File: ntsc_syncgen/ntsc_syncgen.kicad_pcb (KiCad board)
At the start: 2 copper layers, 7 parts, among them U1 74HC4040D, U2 74HC4040D, U3 74HC7014, U4 74HC74D, Y1 Crystal

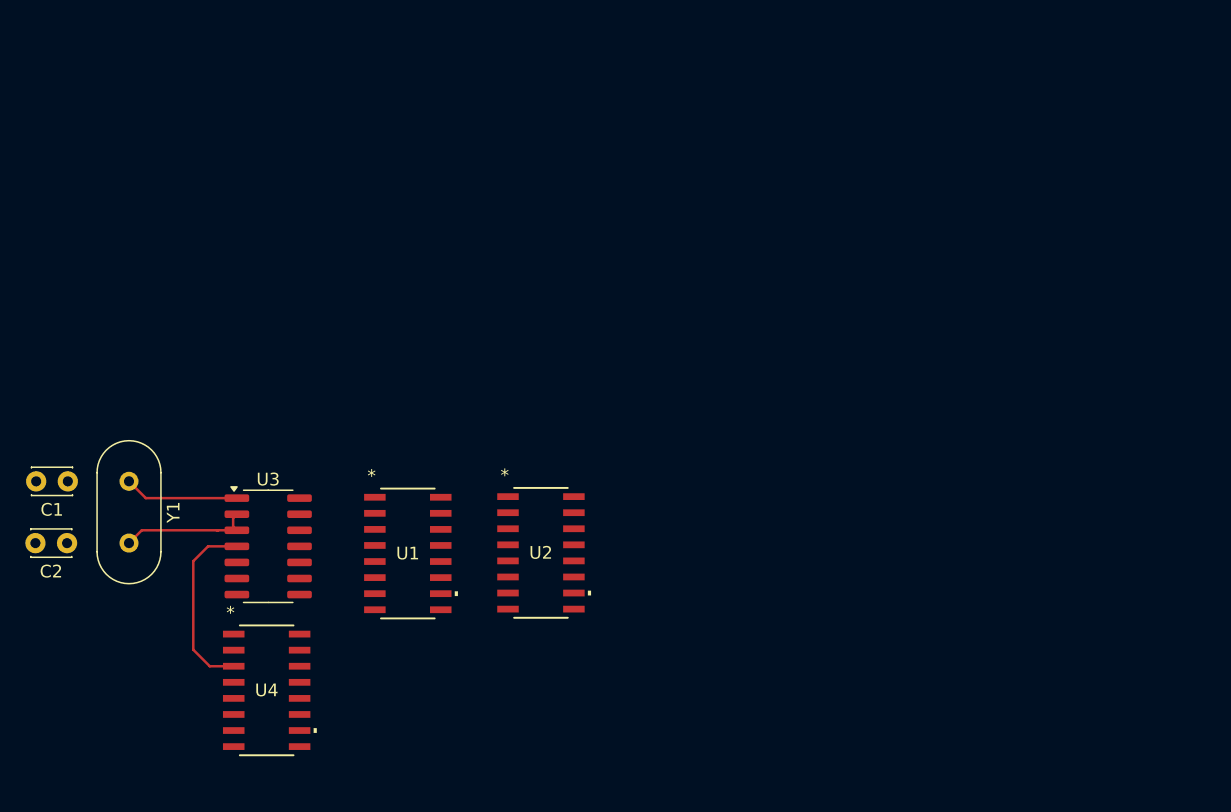
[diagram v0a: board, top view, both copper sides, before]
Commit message: example circuit
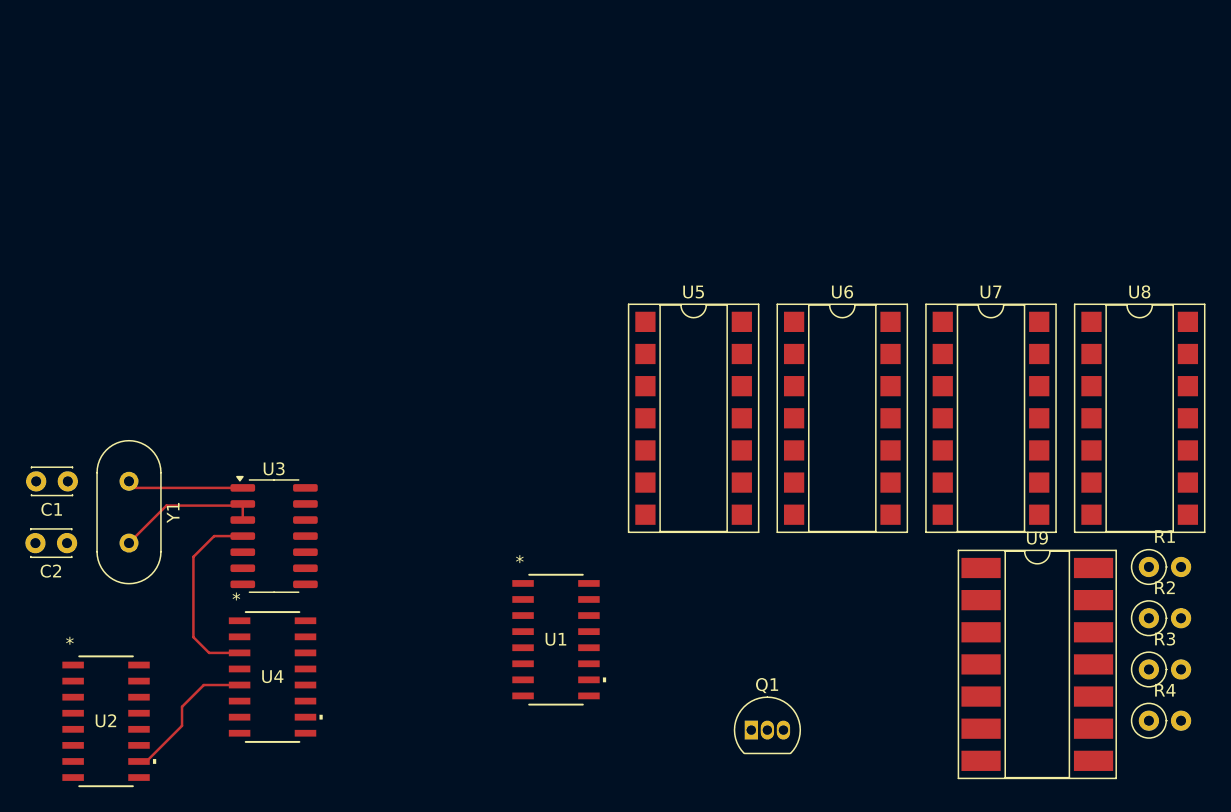
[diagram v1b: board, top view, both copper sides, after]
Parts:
- added Q1: PN2222A, Package_TO_SOT_THT:TO-92_Inline, F.Cu at (148.8, 103.6)
- added R1: R, Resistor_THT:R_Axial_DIN0207_L6.3mm_D2.5mm_P2.54mm_Vertical, F.Cu at (180.2, 90.8)
- added R2: R, Resistor_THT:R_Axial_DIN0207_L6.3mm_D2.5mm_P2.54mm_Vertical, F.Cu at (180.2, 94.8)
- added R3: R, Resistor_THT:R_Axial_DIN0207_L6.3mm_D2.5mm_P2.54mm_Vertical, F.Cu at (180.2, 98.8)
- added R4: R, Resistor_THT:R_Axial_DIN0207_L6.3mm_D2.5mm_P2.54mm_Vertical, F.Cu at (180.2, 102.9)
- added U5: 74HC00, Package_DIP:DIP-14_W7.62mm_SMDSocket_SmallPads, F.Cu at (144.2, 79.0)
- added U6: 4081, Package_DIP:DIP-14_W7.62mm_SMDSocket_SmallPads, F.Cu at (156.0, 79.0)
- added U7: 4081, Package_DIP:DIP-14_W7.62mm_SMDSocket_SmallPads, F.Cu at (167.7, 79.0)
- added U8: 4081, Package_DIP:DIP-14_W7.62mm_SMDSocket_SmallPads, F.Cu at (179.5, 79.0)
- added U9: 4001, Package_DIP:DIP-14_W8.89mm_SMDSocket_LongPads, F.Cu at (171.4, 98.5)
- moved U2 36.9 mm to (97.8, 102.9)
- moved U1 13.5 mm to (133.4, 96.5)
- moved U4 1.15 mm to (111.0, 99.4)
- moved U3 0.93 mm to (111.1, 88.3)
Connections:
- net Net-(U4-1CP) renamed 14.318mhz_CLK0
- U1 pad 10: unconnected-(U1-CP*-Pad10) -> H_RESET
- U1 pad 12: unconnected-(U1-Q8-Pad12) -> 128V
- U1 pad 13: unconnected-(U1-Q7-Pad13) -> 64V
- U1 pad 14: unconnected-(U1-Q9-Pad14) -> 256V
- U1 pad 15: unconnected-(U1-Q10-Pad15) -> 512V
- U1 pad 2: unconnected-(U1-Q5-Pad2) -> 16V
- U1 pad 3: unconnected-(U1-Q4-Pad3) -> 8V
- U1 pad 4: unconnected-(U1-Q6-Pad4) -> 32V
- U1 pad 5: unconnected-(U1-Q3-Pad5) -> 4V
- U1 pad 6: unconnected-(U1-Q2-Pad6) -> 2V
- U1 pad 7: unconnected-(U1-Q1-Pad7) -> 1V
- U2 pad 10: unconnected-(U2-CP*-Pad10) -> 7.1mhz_CLK1
- U2 pad 12: unconnected-(U2-Q8-Pad12) -> 128H
- U2 pad 13: unconnected-(U2-Q7-Pad13) -> 64H
- U2 pad 14: unconnected-(U2-Q9-Pad14) -> 256H
- U2 pad 15: unconnected-(U2-Q10-Pad15) -> 512H
- U2 pad 2: unconnected-(U2-Q5-Pad2) -> 16H
- U2 pad 3: unconnected-(U2-Q4-Pad3) -> 8H
- U2 pad 4: unconnected-(U2-Q6-Pad4) -> 32H
- U2 pad 5: unconnected-(U2-Q3-Pad5) -> 4H
- U2 pad 6: unconnected-(U2-Q2-Pad6) -> 2H
- U2 pad 7: unconnected-(U2-Q1-Pad7) -> 1H
- U4 pad 5: unconnected-(U4-1Q-Pad5) -> 7.1mhz_CLK1
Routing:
- net 7.1mhz_CLK1: track 0.00 -> 11.3 mm
- net Net-(C2-Pad1): track 10.6 -> 11.5 mm

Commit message: more work
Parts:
- added U10: 74HC74, Library:SOIC127P600X175-14N, F.Cu at (109.3, 54.6)
- added U4: 74HC74D, footprints:SOT109-1_NXP, F.Cu at (98.8, 55.1)
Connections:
- U1 pad 12: 128V -> 256V
- U1 pad 13: 64V -> 128V
- U1 pad 14: 256V -> 512V
- U1 pad 15: 512V -> unconnected-(U1-Q10-Pad15)
- U1 pad 2: 16V -> 32V
- U1 pad 3: 8V -> 16V
- U1 pad 4: 32V -> 64V
- U1 pad 5: 4V -> 8V
- U1 pad 6: 2V -> 4V
- U1 pad 7: 1V -> 2V
- U1 pad 9: unconnected-(U1-Q0-Pad9) -> 1V
- U2 pad 10: 7.1mhz_CLK1 -> 14.318mhz_CLK0
- U2 pad 11: unconnected-(U2-MR-Pad11) -> H_RESET
- U2 pad 9: unconnected-(U2-Q0-Pad9) -> 7.1mhz_CLK1
- U7 pad 1: unconnected-(U7-Pad1) -> 2H
- U7 pad 11: unconnected-(U7-Pad11) -> Net-(U7-Pad11)
- U7 pad 12: unconnected-(U7-Pad12) -> Net-(U7-Pad12)
- U7 pad 13: unconnected-(U7-Pad13) -> 256H
- U7 pad 2: unconnected-(U7-Pad2) -> 4H
- U7 pad 3: unconnected-(U7-Pad3) -> Net-(U7-Pad3)
- U7 pad 4: unconnected-(U7-Pad4) -> Net-(U7-Pad12)
- U7 pad 5: unconnected-(U7-Pad5) -> 64H
- U7 pad 6: unconnected-(U7-Pad6) -> 128H
- U7 pad 8: unconnected-(U7-Pad8) -> Net-(U7-Pad3)
- U7 pad 9: unconnected-(U7-Pad9) -> Net-(U7-Pad11)
